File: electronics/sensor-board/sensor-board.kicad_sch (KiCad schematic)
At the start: 40 parts

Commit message: edited sensor-board
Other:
- added sheet Op Amp Array 1 (op_amp_array_1.kicad_sch)
- note added: "(single ended) input"
- note added: "Add sensor supplies"
- note added: "regulator, voltage divider... low impedence"
- note removed: "1/2vcc, regulator, voltage divider... low impedence"
- note removed: "inverting (single ended) input"
- moved on the sheet: C?, R?, U?

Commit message: sensor-board layout edit
op amp subunits added
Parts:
- removed C?: 0.1uF, symbol Device:C_Polarized
- removed R? (x2): R, symbol Device:R
- removed R? (x2): same_as_R1, symbol Device:R
- removed R? (x2): same_as_R2, symbol Device:R
- removed U?: OPA4197QPWRQ1, TSSOP_QPWRQ1_TEX, symbol OPA4197QPWRQ1:OPA4197QPWRQ1
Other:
- added sheet Op Amp Array 2 (op_amp_array_2.kicad_sch)
- added sheet Op Amp Array 3 (op_amp_array_3.kicad_sch)
- added sheet Op Amp Array 4 (op_amp_array_4.kicad_sch)
- added sheet Op Amp Array 5 (op_amp_array_5.kicad_sch)
- sheet Op Amp Array 1 ports: added VDD, VSS, diff+A, diff+B, diff+C, diff+D, diff-A, diff-B, diff-C, diff-D, output_A, output_B, output_C, output_D; removed input_bus, output_bus, power
- note removed: "(single ended) input"
- note removed: "Inv. Diff. Input"
- note removed: "Non-Inv. Diff. Input"
- note removed: "output"
- note removed: "regulator, voltage divider... low impedence"
- moved on the sheet: J?, U?

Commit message: sensor-board edit
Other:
- added sheet Op Amp Array 6 (op_amp_array_6_lmc6036.kicad_sch)

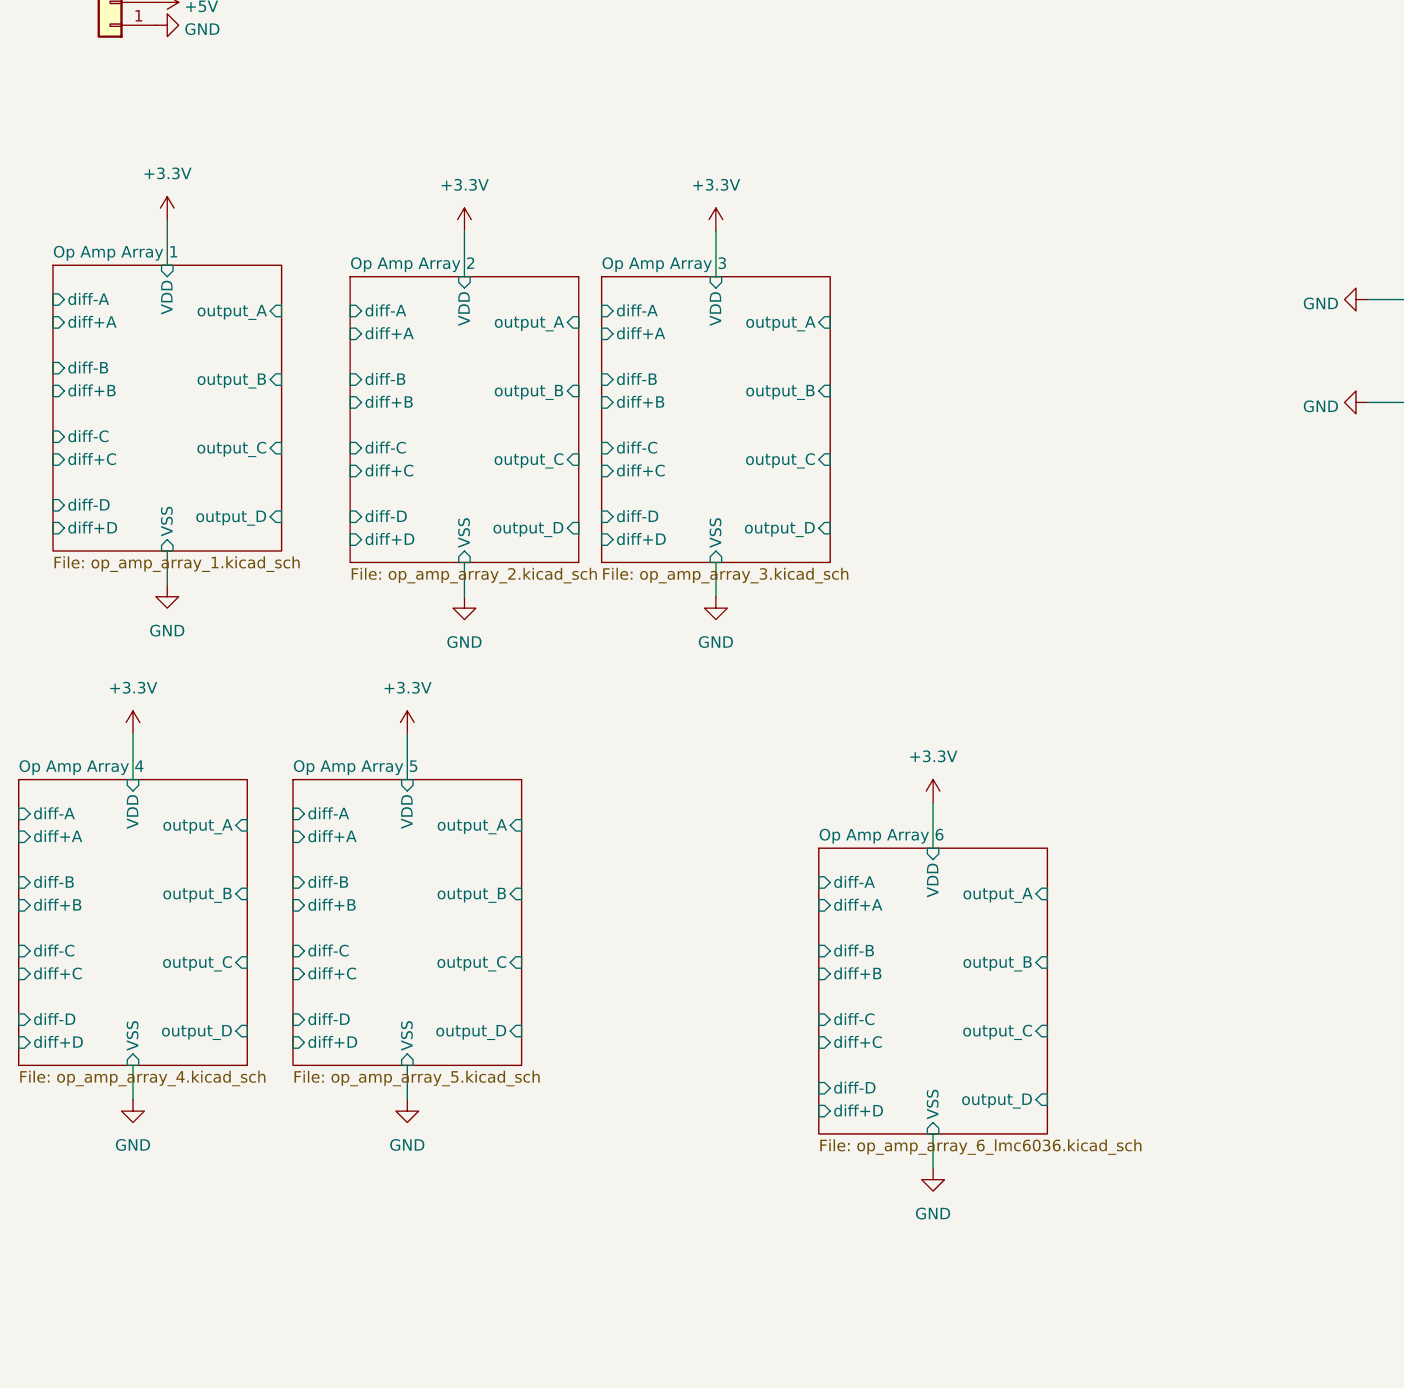
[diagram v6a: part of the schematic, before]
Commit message: sensor-board edits
Finalized pressure and flow sensor circuits.
Reorganized schematics
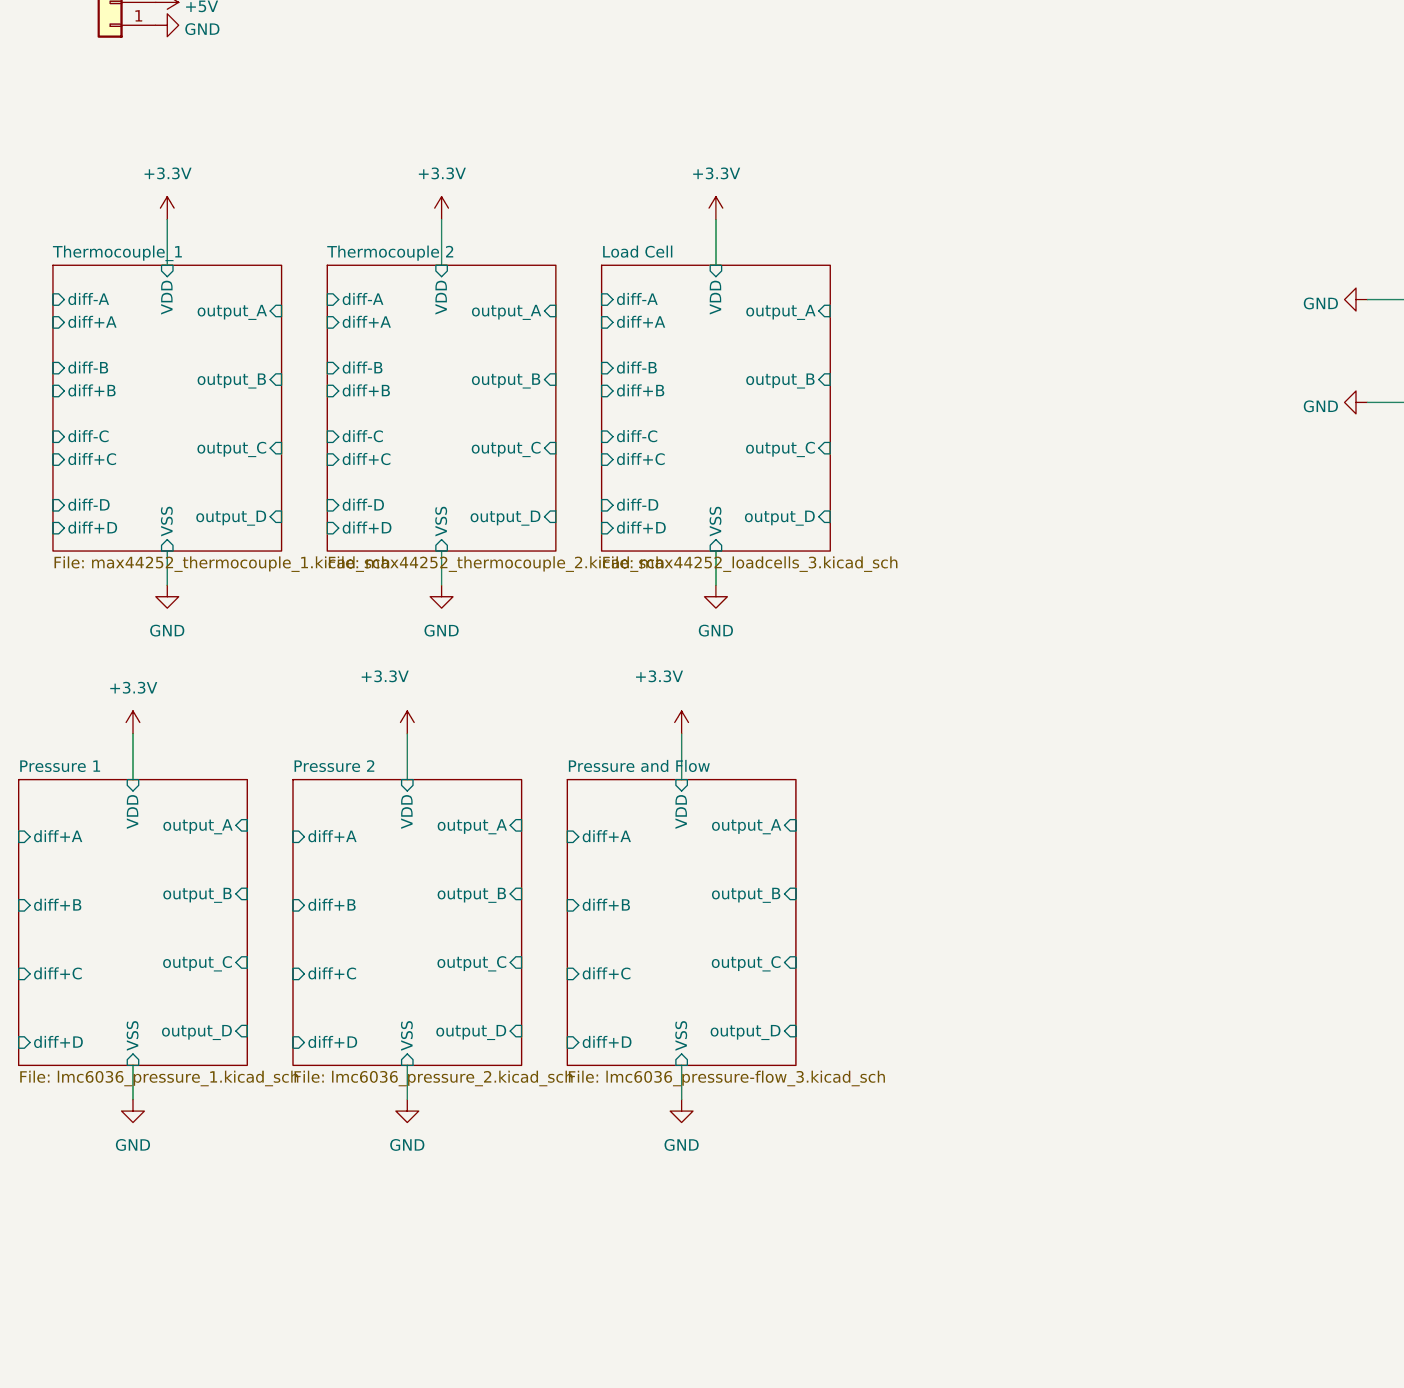
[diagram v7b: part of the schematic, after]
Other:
- sheet Op Amp Array 1 renamed Thermocouple_1
- sheet Op Amp Array 2 renamed Thermocouple 2
- sheet Op Amp Array 3 renamed Load Cell
- sheet Op Amp Array 4 renamed Pressure 1
- sheet Op Amp Array 5 renamed Pressure 2
- sheet Op Amp Array 6 renamed Pressure and Flow
- sheet Load Cell: file op_amp_array_3.kicad_sch -> max44252_loadcells_3.kicad_sch
- sheet Pressure 1: file op_amp_array_4.kicad_sch -> lmc6036_pressure_1.kicad_sch
- sheet Pressure 1 ports: added none; removed diff-A, diff-B, diff-C, diff-D
- sheet Pressure 2: file op_amp_array_5.kicad_sch -> lmc6036_pressure_2.kicad_sch
- sheet Pressure 2 ports: added none; removed diff-A, diff-B, diff-C, diff-D
- sheet Pressure and Flow: file op_amp_array_6_lmc6036.kicad_sch -> lmc6036_pressure-flow_3.kicad_sch
- sheet Pressure and Flow ports: added none; removed diff-A, diff-B, diff-C, diff-D
- sheet Thermocouple 2: file op_amp_array_2.kicad_sch -> max44252_thermocouple_2.kicad_sch
- sheet Thermocouple_1: file op_amp_array_1.kicad_sch -> max44252_thermocouple_1.kicad_sch

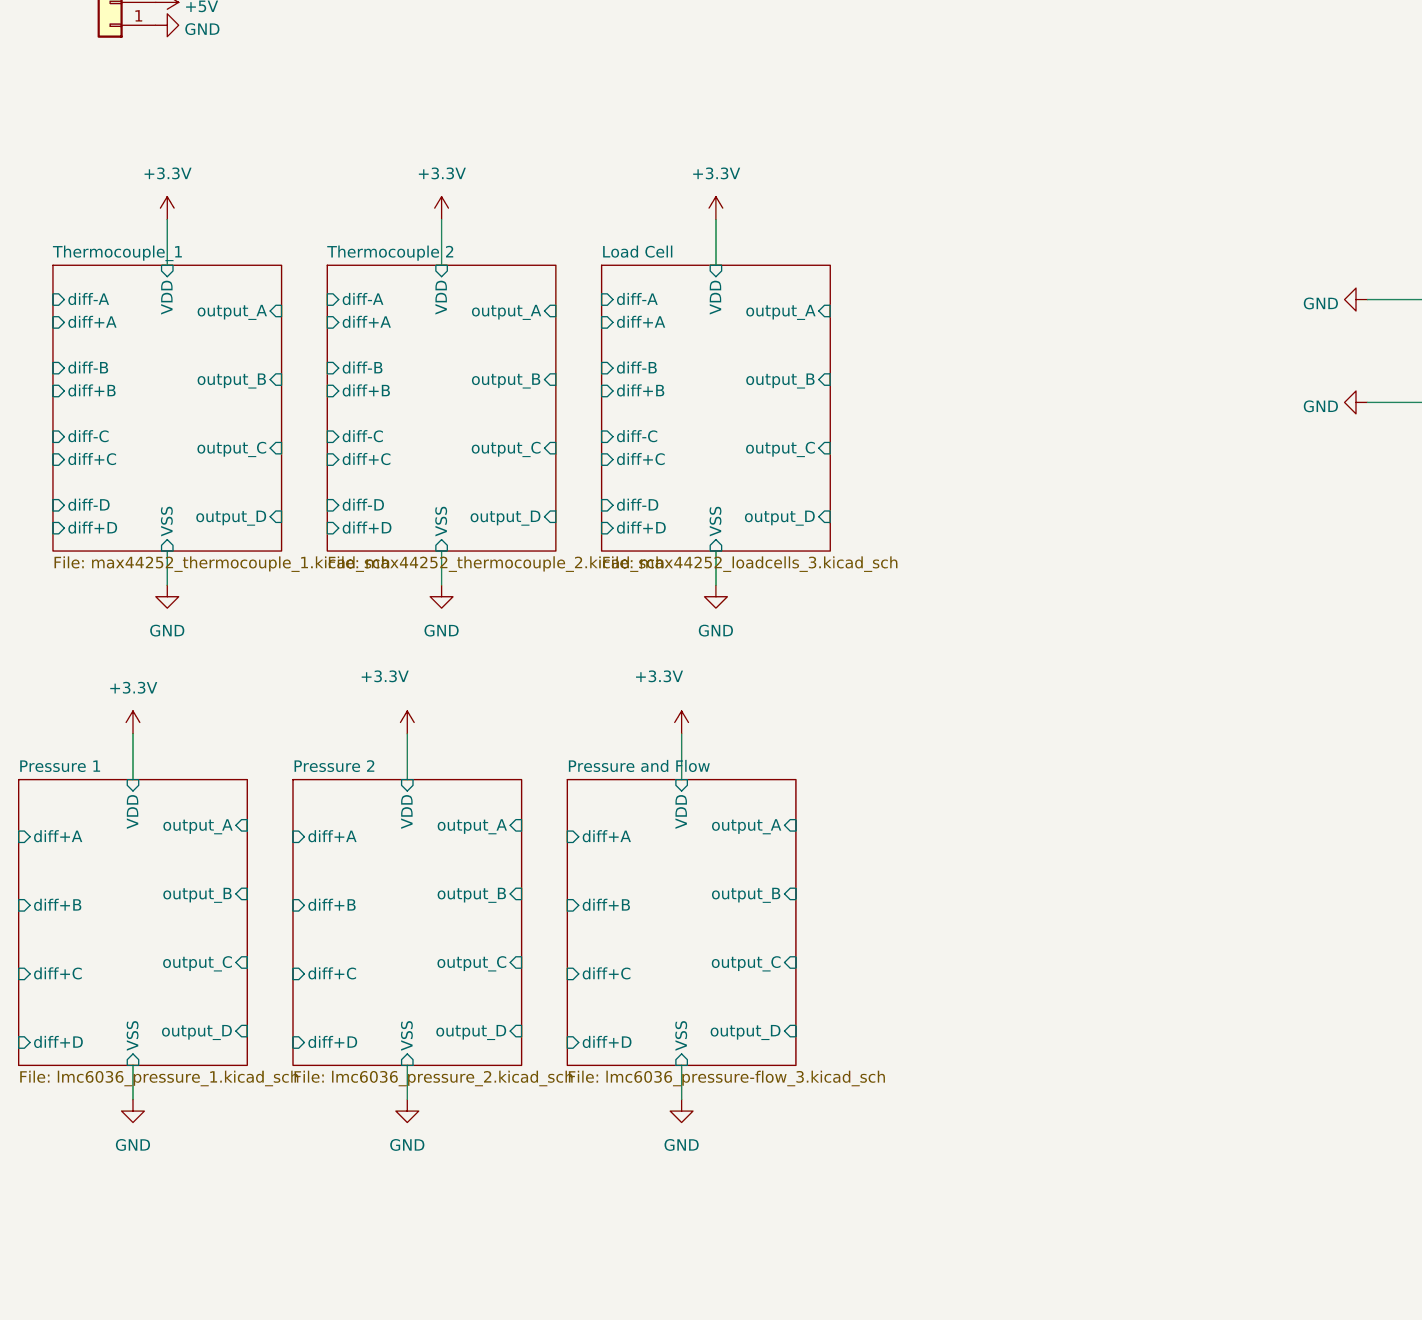
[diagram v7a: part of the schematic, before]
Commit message: added datasheets
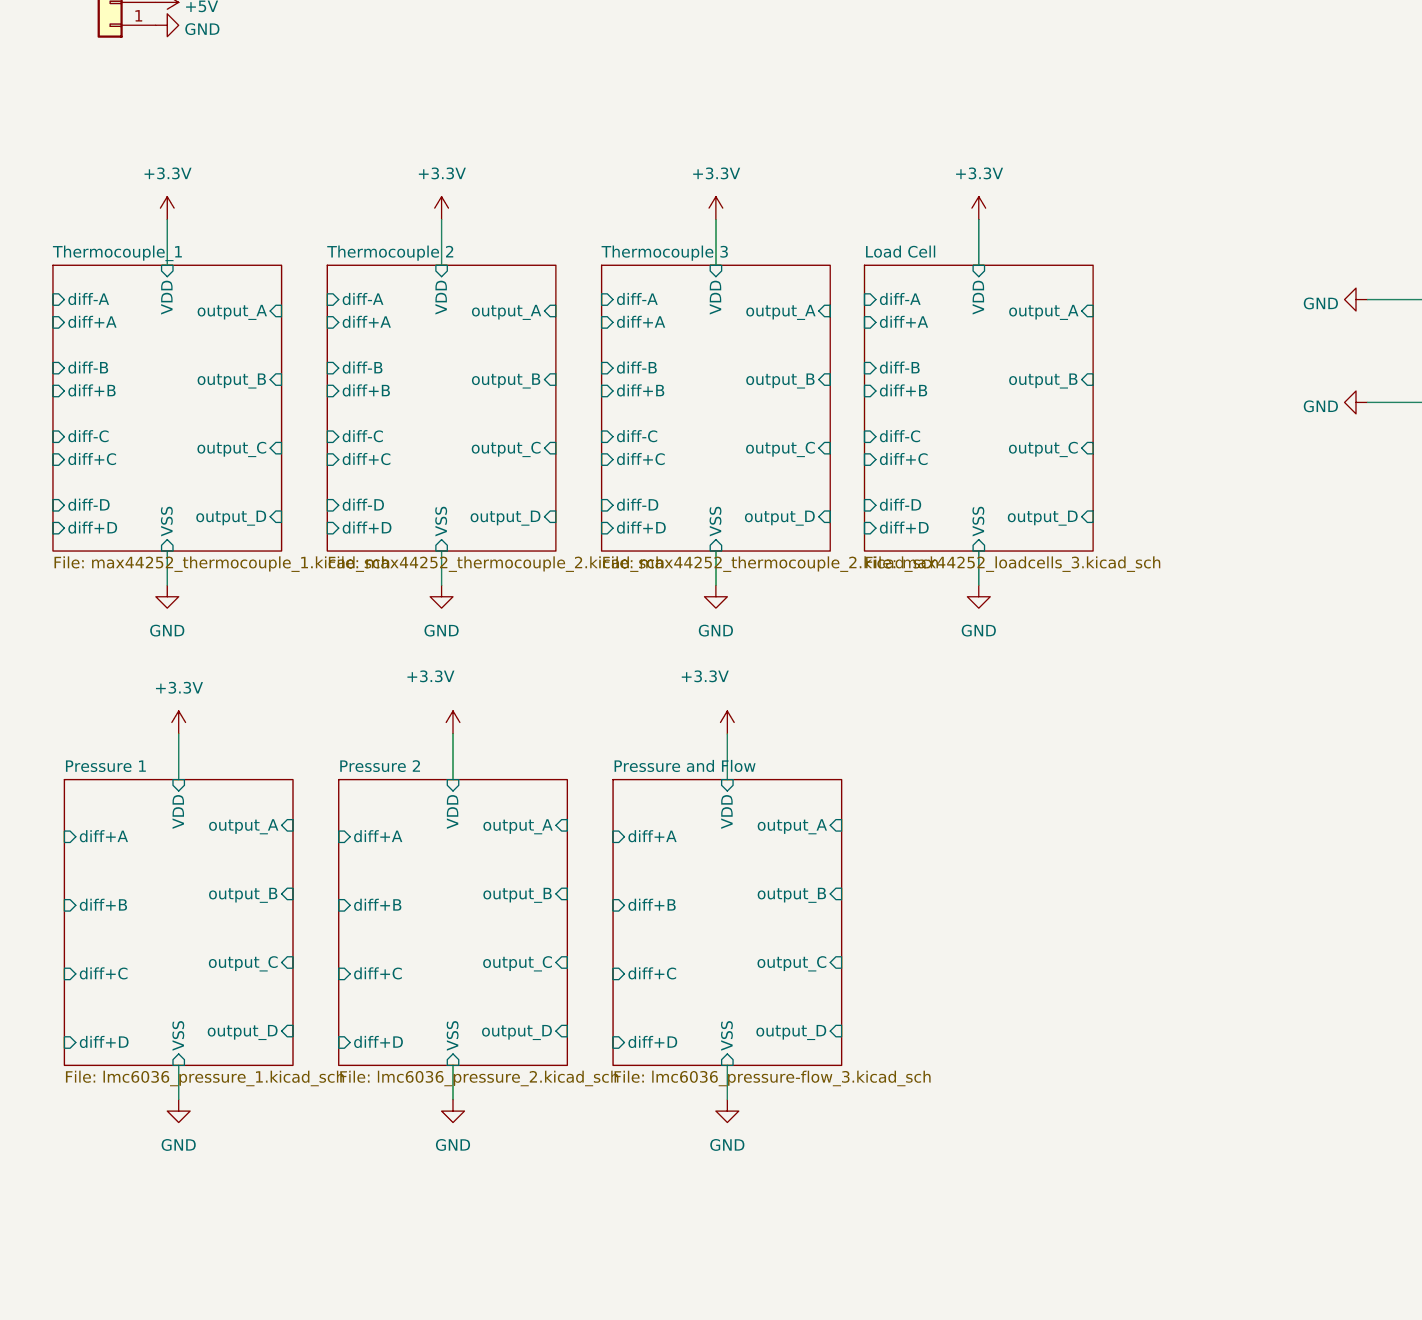
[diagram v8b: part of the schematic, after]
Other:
- added sheet Thermocouple 3 (max44252_thermocouple_2.kicad_sch)
